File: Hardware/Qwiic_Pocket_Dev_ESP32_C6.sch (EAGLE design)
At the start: 53 parts, among them J1 USB Female Type C Connector, J4 QWIIC_RIGHT_ANGLE, Q1 20V/4.2A/52mΩ/1.4W, U1 ESP32-C6-MINI-1, U2 RT9080-33GJ5, U3 MCP73831

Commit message: Add note about SHLD jumper
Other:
- note added: "Cut SHLD jumper to disconnect shield from GND"
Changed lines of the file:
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@@
 BOOT button when ESP32
 resets or powers on</text>
+<text x="15.24" y="142.24" size="1.778" layer="97" font="vector" align="center">Cut SHLD jumper
+to disconnect
+shield from GND</text>
 </plain>
 <instances>

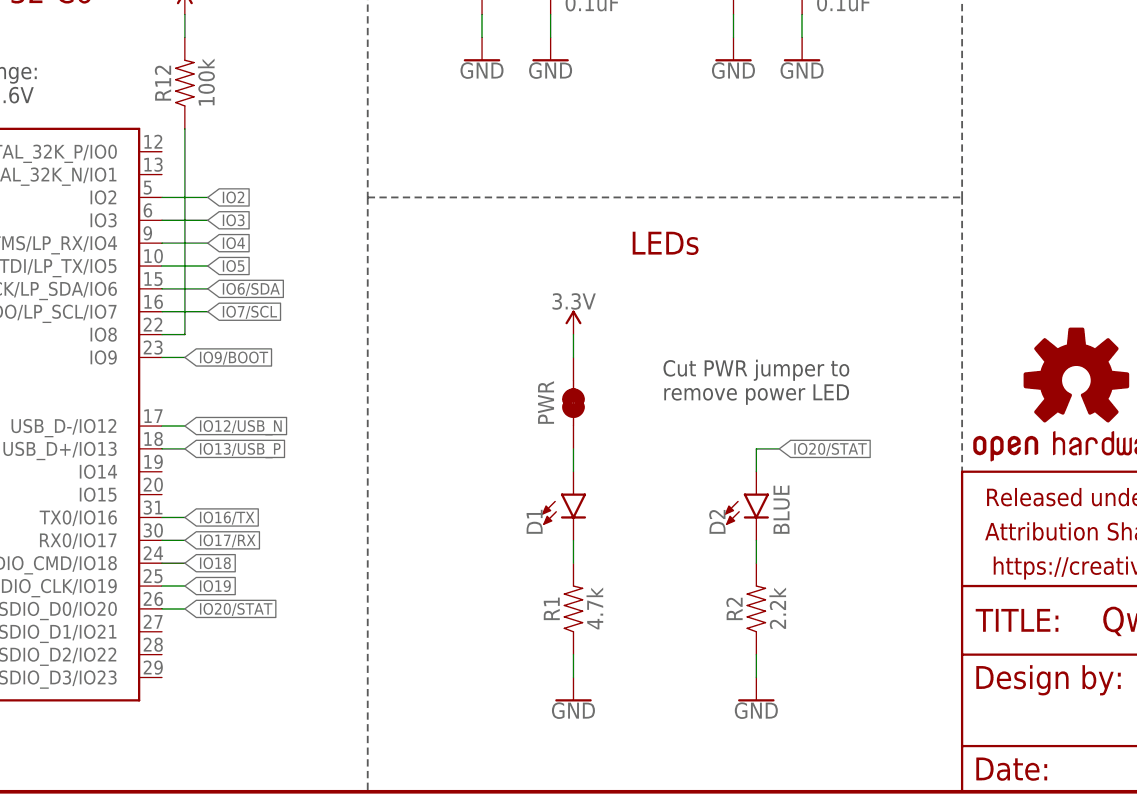
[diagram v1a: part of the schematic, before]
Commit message: Add battery voltage divider
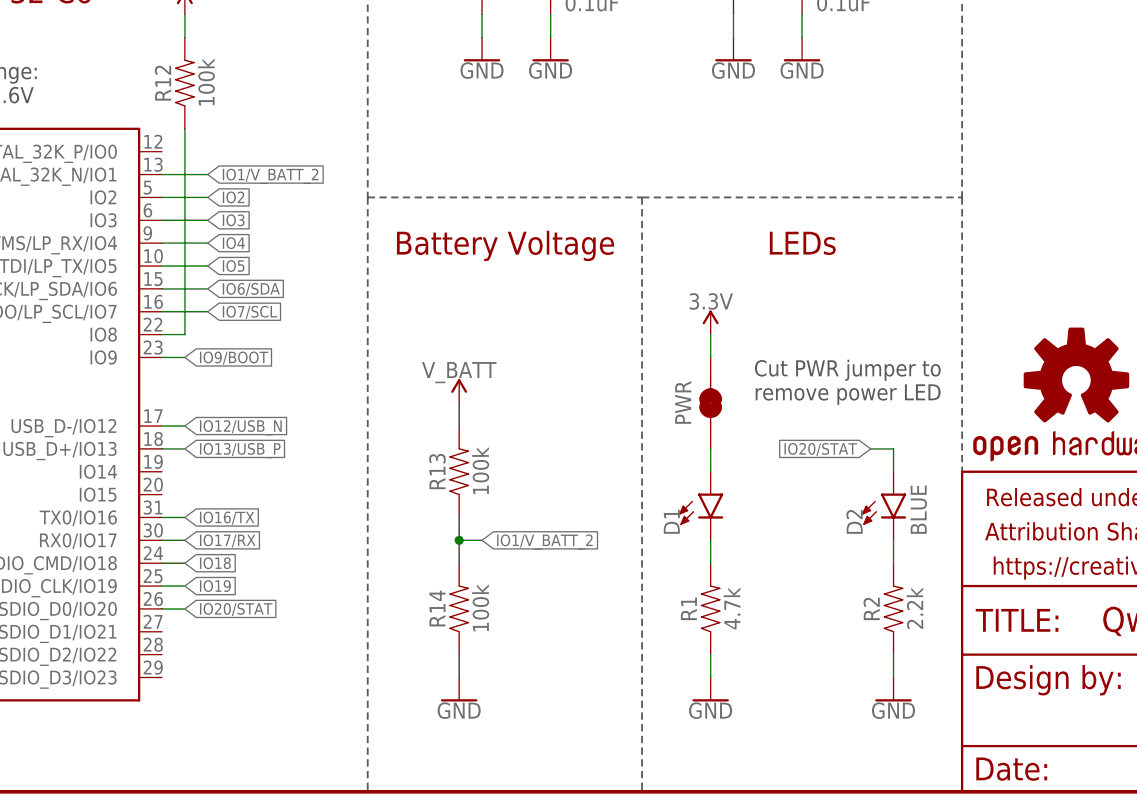
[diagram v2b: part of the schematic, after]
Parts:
- added R13, R14: 100k, SparkFun-Resistors:100KOHM-0402T-1/16W-1%
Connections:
- new net IO1/V_BATT_2: R13.1, R14.2, U1.XTAL_32K_N/IO1
- net GND: now also R14.1
- net V_BATT: now also R13.2
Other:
- note added: "Battery Voltage"
- moved on the sheet: D1, D2, PWR, R1, R2

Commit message: Change STAT LED to GPIO23
GPIO20 likes to magically start toggling the LED when touching GPIO19. Something to do with the SDIO pins, I think
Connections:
- removed net IO20/STAT: D2.A, U1.SDIO_D0/IO20
- new net IO23/STAT: D2.A, U1.SDIO_D3/IO23
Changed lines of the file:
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@@
 </segment>
 </net>
-<net name="IO20/STAT" class="0">
-<segment>
-<pinref part="U1" gate="G$1" pin="SDIO_D0/IO20"/>
-<wire x1="58.42" y1="20.32" x2="60.96" y2="20.32" width="0.1524" layer="91"/>
-<label x="60.96" y="20.32" size="1.27" layer="95" font="vector" xref="yes"/>
-</segment>
+<net name="IO23/STAT" class="0">
 <segment>
 <wire x1="139.7" y1="38.1" x2="137.16" y2="38.1" width="0.1524" layer="91"/>
@@
 <wire x1="139.7" y1="35.56" x2="139.7" y2="38.1" width="0.1524" layer="91"/>
 </segment>
+<segment>
+<wire x1="58.42" y1="12.7" x2="60.96" y2="12.7" width="0.1524" layer="91"/>
+<label x="60.96" y="12.7" size="1.27" layer="95" font="vector" xref="yes"/>
+<pinref part="U1" gate="G$1" pin="SDIO_D3/IO23"/>
+</segment>
 </net>

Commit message: v10 updates
Bump version number
Update STAT LED IO silk label
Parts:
- FRAME1: REV v01 -> v10
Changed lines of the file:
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@@
 <part name="FRAME1" library="SparkFun-Aesthetics" deviceset="FRAME-LETTER" device="">
 <attribute name="DESIGNER" value="Dryw Wade"/>
-<attribute name="REV" value="v01"/>
+<attribute name="REV" value="v10"/>
 </part>
 <part name="GND4" library="SparkFun-PowerSymbols" deviceset="GND" device=""/>

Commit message: Change battery voltage divider resistors to 1M Ohm
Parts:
- R13, R14: value 100k -> 1M; device SparkFun-Resistors:100KOHM-0402T-1/16W-1% -> SparkFun-Resistors:1MOHM-0402T-1/16W-5%
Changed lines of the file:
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@@
 <part name="TP3" library="SparkFun-Connectors" deviceset="TEST-POINT" device="3" value="TEST-POINT3"/>
 <part name="TP4" library="SparkFun-Connectors" deviceset="TEST-POINT" device="3" value="TEST-POINT3"/>
-<part name="R13" library="SparkFun-Resistors" deviceset="100KOHM" device="-0402T-1/16W-1%" value="100k"/>
-<part name="R14" library="SparkFun-Resistors" deviceset="100KOHM" device="-0402T-1/16W-1%" value="100k"/>
+<part name="R13" library="SparkFun-Resistors" deviceset="1MOHM" device="-0402T-1/16W-5%" value="1M"/>
+<part name="R14" library="SparkFun-Resistors" deviceset="1MOHM" device="-0402T-1/16W-5%" value="1M"/>
 <part name="SUPPLY16" library="SparkFun-PowerSymbols" deviceset="V_BATT" device=""/>
 <part name="GND23" library="SparkFun-PowerSymbols" deviceset="GND" device=""/>

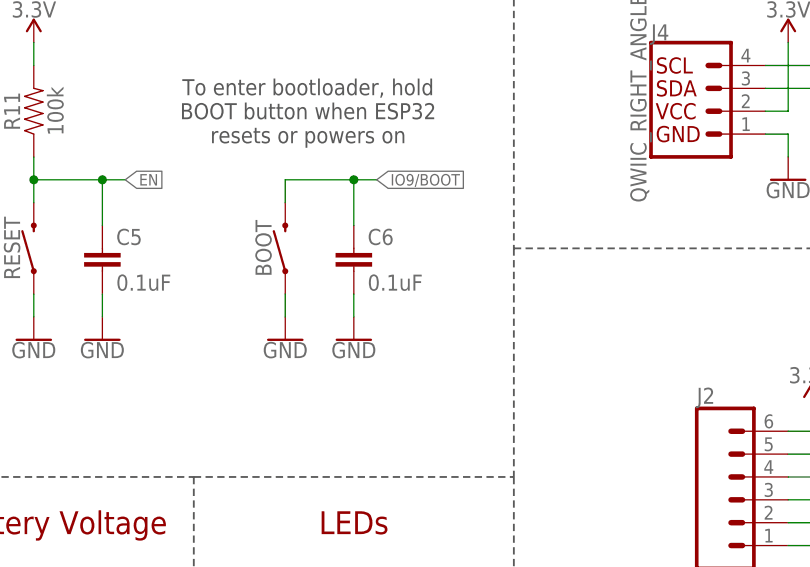
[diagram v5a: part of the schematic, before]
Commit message: Change C6 to DNP
Rise time was slow, causing chip to run bootloader instead of booting from flash
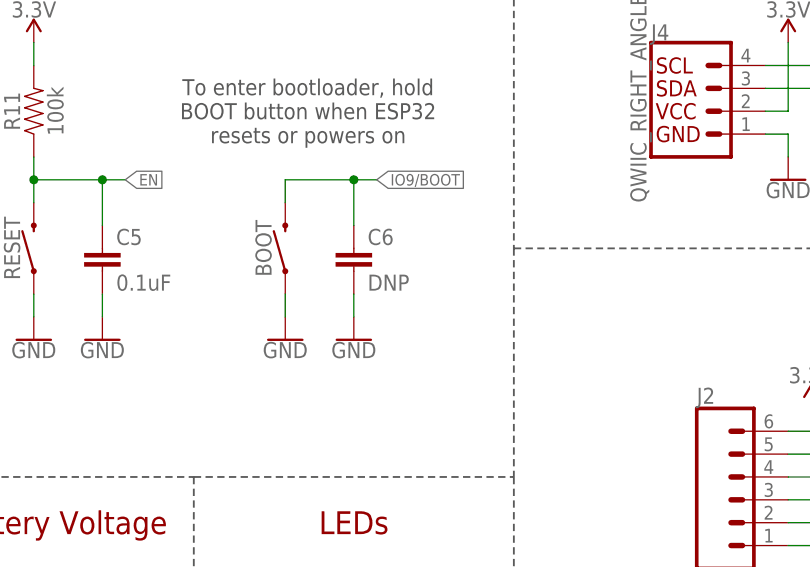
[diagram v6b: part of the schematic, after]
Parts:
- C6: value 0.1uF -> DNP
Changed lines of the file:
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@@
 <part name="SUPPLY12" library="SparkFun-PowerSymbols" deviceset="3.3V" device=""/>
 <part name="GND21" library="SparkFun-PowerSymbols" deviceset="GND" device=""/>
-<part name="C6" library="SparkFun-Capacitors" deviceset="0.1UF" device="-0402T-6.3V-10%-X7R" value="0.1uF"/>
+<part name="C6" library="SparkFun-Capacitors" deviceset="0.1UF" device="-0402T-6.3V-10%-X7R" value="DNP">
+<attribute name="PROD_ID" value=""/>
+</part>
 <part name="GND22" library="SparkFun-PowerSymbols" deviceset="GND" device=""/>
 <part name="R12" library="SparkFun-Resistors" deviceset="100KOHM" device="-0402T-1/16W-1%" value="100k"/>
